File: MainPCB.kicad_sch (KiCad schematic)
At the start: 41 parts, among them J1 RaspberryPi, J10 Conn_01x02, J2 Conn_01x03, J3 Screw_Terminal_01x02, J4 Conn_01x02, J5 Conn_01x06, J6 Conn_01x03_Pin, J7 Conn_01x10, J8 Conn_01x12, J9 Conn_01x04, M1 Motor_DC, M2 Motor_DC, M3 Motor_DC, M4 Motor_DC, SW1 SW_SPDT, SW2 SW_SPDT, SW3 SW_SPDT, SW4 SW_SPDT, SW5 SW_SPDT, SW6 SW_SPDT, SW7 SW_SPDT, U1 Teensy4.1, U10 Compass, U11 V_Regulator5v, U12 RockerSwitch, U13 V_Regulator3.3v, U2 VNH Driver, U3 VNH Driver, U4 VNH Driver, U5 VNH Driver, U6 TSOP25xx

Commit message: Finshined again
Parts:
- added J11: Conn_01x07, Connector_PinHeader_2.54mm:PinHeader_1x07_P2.54mm_Vertical, symbol Connector_Generic:Conn_01x07
- added R2, R3, R4, R5, R6, R7, R8: 10k, Capacitor_SMD:C_0805_2012Metric_Pad1.18x1.45mm_HandSolder, symbol Device:R
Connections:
- net 3.3V: no longer J7.1 (Pin_1), U1.46 (3V3)
- net 5V: now also J7.1 (Pin_1)
- net ECHO1: now also U1.26 (34_RX8)
- net ECHO2: now also U1.28 (36_CS)
- net ECHO3: now also U1.30 (38_CS1_IN1)
- net ECHO4: now also U1.32 (40_A16)
- net GND: now also R2.2, R3.2, R4.2, R5.2, R6.2, R7.2, R8.2
- net SLIDE1: now also U1.23 (31_CTX3), J11.7 (Pin_7), R2.1; no longer U1.32 (40_A16)
- net SLIDE2: now also J11.6 (Pin_6), R3.1; no longer U1.31 (39_MISO1_OUT1A)
- net SLIDE3: now also J11.5 (Pin_5), R4.1; no longer U1.30 (38_CS1_IN1)
- net SLIDE4: now also J11.4 (Pin_4), R5.1; no longer U1.29 (37_CS)
- net SLIDE5: now also J11.3 (Pin_3), R6.1; no longer U1.28 (36_CS)
- net SLIDE6: now also J11.2 (Pin_2), R7.1; no longer U1.27 (35_TX8)
- net SLIDE7: now also J11.1 (Pin_1), R8.1; no longer U1.26 (34_RX8)
- net STATE: no longer U1.23 (31_CTX3)
- net TRIG1: now also U1.25 (33_MCLK2)
- net TRIG2: now also U1.27 (35_TX8)
- net TRIG3: now also U1.29 (37_CS)
- net TRIG4: now also U1.31 (39_MISO1_OUT1A)
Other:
- moved on the sheet: H4, H7

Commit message: part movement
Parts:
- removed J11: Conn_01x07, Connector_PinHeader_2.54mm:PinHeader_1x07_P2.54mm_Vertical, symbol Connector_Generic:Conn_01x07
- removed J7: Conn_01x10, Connector_IDC:IDC-Header_2x05_P2.54mm_Vertical, symbol Connector_Generic:Conn_01x10
- removed R6, R7, R8: 10k, Capacitor_SMD:C_0805_2012Metric_Pad1.18x1.45mm_HandSolder, symbol Device:R
- removed SW5, SW6, SW7: SW_SPDT, SlideSW:SPDT_OS102011_CNK, symbol Switch:SW_SPDT
- added J12: Conn_01x07, Connector_IDC:IDC-Header_2x04_P2.54mm_Vertical, symbol Connector_Generic:Conn_01x07
- H1, H2, H3, H4: footprint MountingHole:MountingHole_3.2mm_M3 -> MountingHole:MountingHole_3.2mm_M3_DIN965_Pad
- H5, H6, H7, H8: footprint MountingHole:MountingHole_2.7mm_M2.5 -> MountingHole:MountingHole_2.7mm_M2.5_DIN965_Pad
- U10: footprint Connector_PinHeader_2.54mm:PinHeader_1x04_P2.54mm_Vertical -> Custom:Compass Sensor DFRobot
- U11, U13: footprint Connector_PinHeader_2.54mm:PinHeader_1x05_P2.54mm_Vertical -> Custom:Pololu Regulator
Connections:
- net ECHO2 is gone; now on net SLIDE2: U1.28 (36_CS)
- net ECHO3 is gone; now on net SLIDE3: U1.30 (38_CS1_IN1)
- net ECHO4 is gone; now on net SLIDE4: U1.32 (40_A16)
- net 5V: now also J12.1 (Pin_1)
- net GND: now also J12.7 (Pin_7)
- net TRIG1: now also J12.2 (Pin_2)
- net TRIG2: now also J12.3 (Pin_3)
- net TRIG3: now also J12.4 (Pin_4)
- net TRIG4: now also J12.5 (Pin_5)
- net ECHO1 renamed ECHO
- net ECHO: now also J12.6 (Pin_6)
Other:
- moved on the sheet: J10, J2, J3, J4, J5, J6, J8, J9, M1, M2, M3, M4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

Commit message: Made Changes
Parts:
- H5, H6, H7, H8: footprint MountingHole:MountingHole_2.7mm_M2.5_DIN965_Pad -> MountingHole:MountingHole_3.2mm_M3_DIN965_Pad
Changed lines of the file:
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@@
 			)
 		)
-		(property "Footprint" "MountingHole:MountingHole_2.7mm_M2.5_DIN965_Pad"
+		(property "Footprint" "MountingHole:MountingHole_3.2mm_M3_DIN965_Pad"
 			(at 127.635 256.54 0)
 			(effects
@@
 			)
 		)
-		(property "Footprint" "MountingHole:MountingHole_2.7mm_M2.5_DIN965_Pad"
+		(property "Footprint" "MountingHole:MountingHole_3.2mm_M3_DIN965_Pad"
 			(at 125.73 237.49 0)
 			(effects
@@
 			)
 		)
-		(property "Footprint" "MountingHole:MountingHole_2.7mm_M2.5_DIN965_Pad"
+		(property "Footprint" "MountingHole:MountingHole_3.2mm_M3_DIN965_Pad"
 			(at 126.365 250.825 0)
 			(effects
@@
 			)
 		)
-		(property "Footprint" "MountingHole:MountingHole_2.7mm_M2.5_DIN965_Pad"
+		(property "Footprint" "MountingHole:MountingHole_3.2mm_M3_DIN965_Pad"
 			(at 125.476 242.824 0)
 			(effects

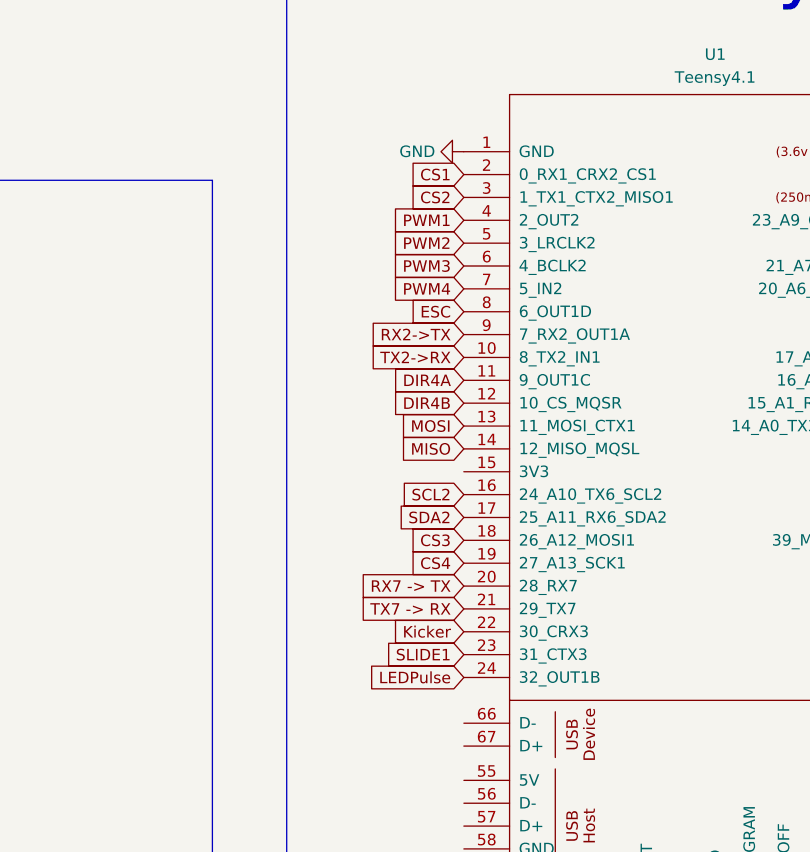
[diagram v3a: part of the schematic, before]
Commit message: Changed LED Pulse pin to PWM
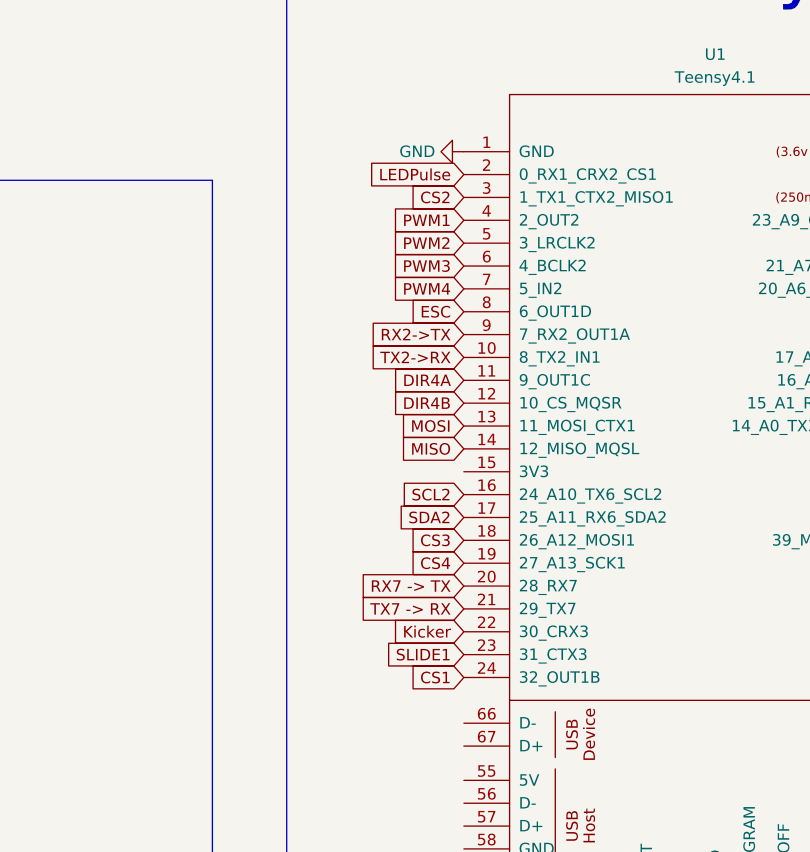
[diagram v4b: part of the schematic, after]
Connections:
- net CS1: now also U1.24 (32_OUT1B); no longer U1.2 (0_RX1_CRX2_CS1)
- net LEDPulse: now also U1.2 (0_RX1_CRX2_CS1); no longer U1.24 (32_OUT1B)

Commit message: Changed Layout
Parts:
- removed J10: Conn_01x02, Connector_JST:JST_XH_B2B-XH-AM_1x02_P2.50mm_Vertical, symbol Connector_Generic:Conn_01x02
- removed J12: Conn_01x07, Connector_IDC:IDC-Header_2x04_P2.54mm_Vertical, symbol Connector_Generic:Conn_01x07
- removed J2: Conn_01x03, Connector_JST:JST_XH_B3B-XH-AM_1x03_P2.50mm_Vertical, symbol Connector_Generic:Conn_01x03
- removed J9: Conn_01x04, Connector_JST:JST_XH_B4B-XH-AM_1x04_P2.50mm_Vertical, symbol Connector_Generic:Conn_01x04
- added C1, C2: 10uf, Capacitor_SMD:C_0805_2012Metric, symbol Device:C
- added C10, C11, C12, C3, C4, C5, C6, C7, C8, C9: .1uf, Capacitor_SMD:C_0805_2012Metric, symbol Device:C
- added J2, J7: Conn_01x05, Connector_JST:JST_XH_B5B-XH-A_1x05_P2.50mm_Vertical, symbol Connector_Generic:Conn_01x05
- added M5: Motor_DC, Connector_JST:JST_XH_B2B-XH-AM_1x02_P2.50mm_Vertical, symbol Motor:Motor_DC
- added NT1, NT2, NT3, NT4, NT5, NT6: NetTie_2, symbol Device:NetTie_2
- added R6: 15k, Capacitor_SMD:C_0805_2012Metric, symbol Device:R
- added R7: 10k, Capacitor_SMD:C_0805_2012Metric, symbol Device:R
- added U7: V_Regulator5v, Custom:Pololu Regulator, symbol Voltage Regulator:V_Regulator_-_5v
- added U8: VNH Driver, MotorDriver:VNHDriver, symbol VNHMotorDriver:MotorDriver
- J3: footprint SMDPads:Pads_1x02_XL -> Connector_AMASS:AMASS_XT60-F_1x02_P7.20mm_Vertical
- J4: footprint Connector_JST:JST_XH_B2B-XH-AM_1x02_P2.50mm_Vertical -> Connector_PinHeader_2.54mm:PinHeader_2x01_P2.54mm_Vertical
- U11: footprint Custom:Pololu Regulator -> Custom:Pololu5V3.4A
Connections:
- net TX4->RX is gone; now on net STATE: U1.39 (17_A3_TX4_SDA1)
- net 12V: now also U7.3 (IN+), U8.1 (12v)
- net 3.3V: now also NT3.2, NT4.1, NT6.1, U8.4 (DIR2); no longer J5.2 (Pin_2), J8.12 (Pin_12), U10.1 (3.3v)
- net 5V: now also NT1.2, NT2.2, NT5.1, U7.5 (OUT+); no longer J1.1 (Pin_1), U1.48 (VIN)
- net ECHO: now also R6.2, R7.1
- net GND: now also C1.2, C10.2, C11.2, C12.2, C2.2, C3.2, C4.2, C5.2, C6.2, C7.2, C8.2, C9.2, J2.2 (Pin_2), J7.2 (Pin_2), R6.1, U7.4 (OUT-), U8.2 (GND), U8.3 (DIR1)
- net TRIG1: now also J2.3 (Pin_3)
- net TRIG2: now also J2.4 (Pin_4)
- net TRIG3: now also J7.3 (Pin_3)
- net TRIG4: now also J7.4 (Pin_4)
- net ESC renamed PWM5
- net PWM5: now also U8.5 (PWM)
- net RX4->TX: no longer names the net of U1.38 (16_A2_RX4_SCL1)
- new net: C10.1, C9.1, J8.12 (Pin_12), NT4.2
- new net: C5.1, C6.1, NT3.1, U10.1 (3.3v)
- new net: C11.1, C12.1, J2.1 (Pin_1), J7.1 (Pin_1), NT6.2
- new net: C7.1, C8.1, J5.2 (Pin_2), NT5.2
- new net: M5.1 (+), U8.6 (OUTA)
- new net: M5.2 (-), U8.7 (OUTB)
- new net: C3.1, C4.1, J1.1 (Pin_1), NT2.1
- new net: C1.1, C2.1, NT1.1, U1.48 (VIN)
- new net: J2.5 (Pin_5), J7.5 (Pin_5), R7.2
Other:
- note removed: "ESC"
- note removed: "OpenMV"
- moved on the sheet: H1, H2, H3, H4, H5, H6, H7, H8, J1, J5, J6, J8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

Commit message: routing
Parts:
- removed NT1, NT2, NT3, NT4, NT5, NT6: NetTie_2, symbol Device:NetTie_2
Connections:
- net 3.3V: now also C10.1, C11.1, C12.1, C5.1, C6.1, C9.1, J2.1 (Pin_1), J7.1 (Pin_1), J8.12 (Pin_12), U10.1 (3.3v)
- net 5V: now also C1.1, C2.1, C3.1, C4.1, C7.1, C8.1, J1.1 (Pin_1), J5.2 (Pin_2), U1.48 (VIN)

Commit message: moved stuff
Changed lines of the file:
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@@
 	(wire
 		(pts
-			(xy 39.37 228.6) (xy 40.64 228.6)
+			(xy 38.1 228.6) (xy 40.64 228.6)
 		)
 		(stroke
@@
 	(global_label "5V"
 		(shape input)
-		(at 39.37 228.6 180)
-		(fields_autoplaced yes)
-		(effects
-			(font
-				(size 1.27 1.27)
-			)
-			(justify right)
-		)
-		(property "Intersheetrefs" "${INTERSHEET_REFS}"
-			(at 34.0867 228.6 0)
-			(effects
-				(font
+		(at 38.1 228.6 180)
+		(fields_autoplaced yes)
+		(effects
+			(font
+				(size 1.27 1.27)
+			)
+			(justify right)
+		)
+		(property "Intersheetrefs" "${INTERSHEET_REFS}"
+			(at 32.8167 228.6 0)
+			(effects
+				(font

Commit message: moved more stuff
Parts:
- added J10, J9: Conn_01x02, Connector_PinHeader_2.54mm:PinHeader_1x02_P2.54mm_Vertical, symbol Connector_Generic:Conn_01x02
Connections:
- net 5V: now also J10.1 (Pin_1), J9.1 (Pin_1)
- net GND: now also J10.2 (Pin_2), J9.2 (Pin_2)
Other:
- note added: "Fans"
